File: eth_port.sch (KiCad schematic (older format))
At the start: 59 parts, among them J301 8P8C_LED_Shielded, U301 LAN8810

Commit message: Exported schematic PDF and BoM, the latter manually massaged. Added a couple missing part #s for big things which seemed important.
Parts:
- TR301: Part# (none) -> PT61020EL
- U301: Part# (none) -> LAN8810-AKZE
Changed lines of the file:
@@
 F 2 "myfp:QFN-72-1EP_10x10mm_P0.5mm_EP6x6mm_ThermalVias" H 4500 3250 50  0001 C CNN
 F 3 "" H 4500 3250 50  0001 C CNN
+F 4 "LAN8810-AKZE" H 4500 3250 50  0001 C CNN "Part#"
 	1    4500 3250
 	1    0    0    -1
@@
 F 2 "myfp:magnetics_PT61020E" H 8300 1450 50  0001 C CNN
 F 3 "" H 8300 2450 50  0001 C CNN
+F 4 "PT61020EL" H 8300 2450 50  0001 C CNN "Part#"
 	1    8300 2450
 	1    0    0    -1
@@
 	1    0    0    -1
 $EndComp
-Wire Bus Line
-	3200 3400 3200 4100
-Wire Bus Line
-	3200 2100 3200 2800
 $Comp
 L Device:C C210
@@
 	1    0    0    -1
 $EndComp
+Wire Bus Line
+	3200 3400 3200 4100
+Wire Bus Line
+	3200 2100 3200 2800
 $EndSCHEMATC

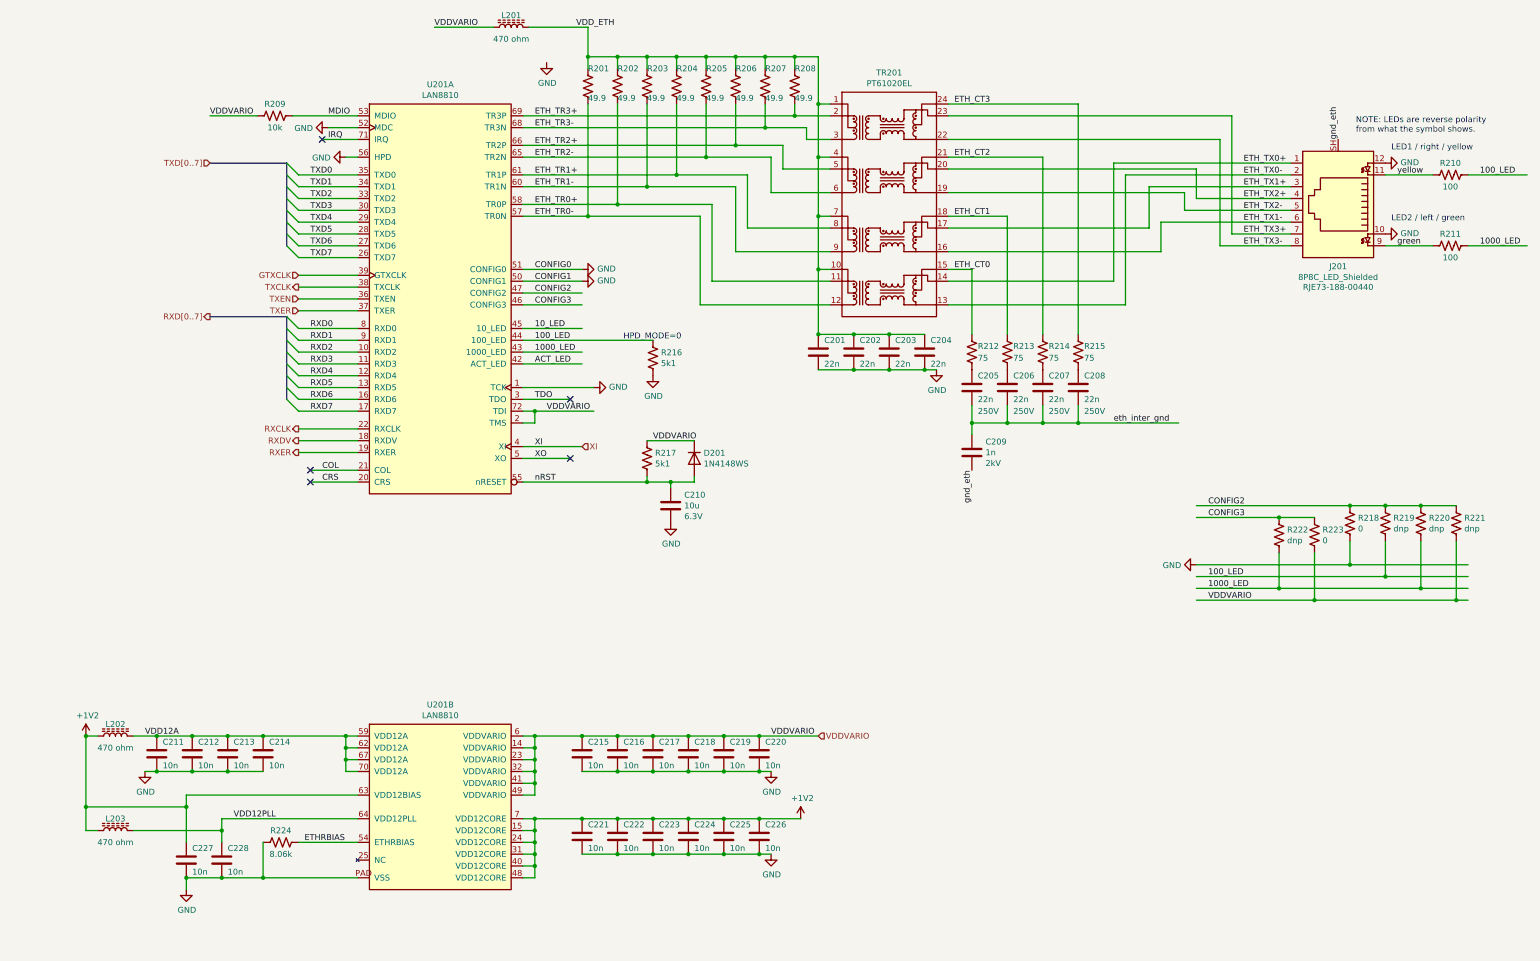
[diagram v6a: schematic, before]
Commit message: Started modifying the schematic to make a different flavor (JVC43B) based on the LAN8831 instead of LAN8810 chip.
This also involved:
- Adding series resistors to the PHY transmit wires (this probably should have
  been there in the A version too)
- Swapped out the 0603 decoupling caps for 0402 ones
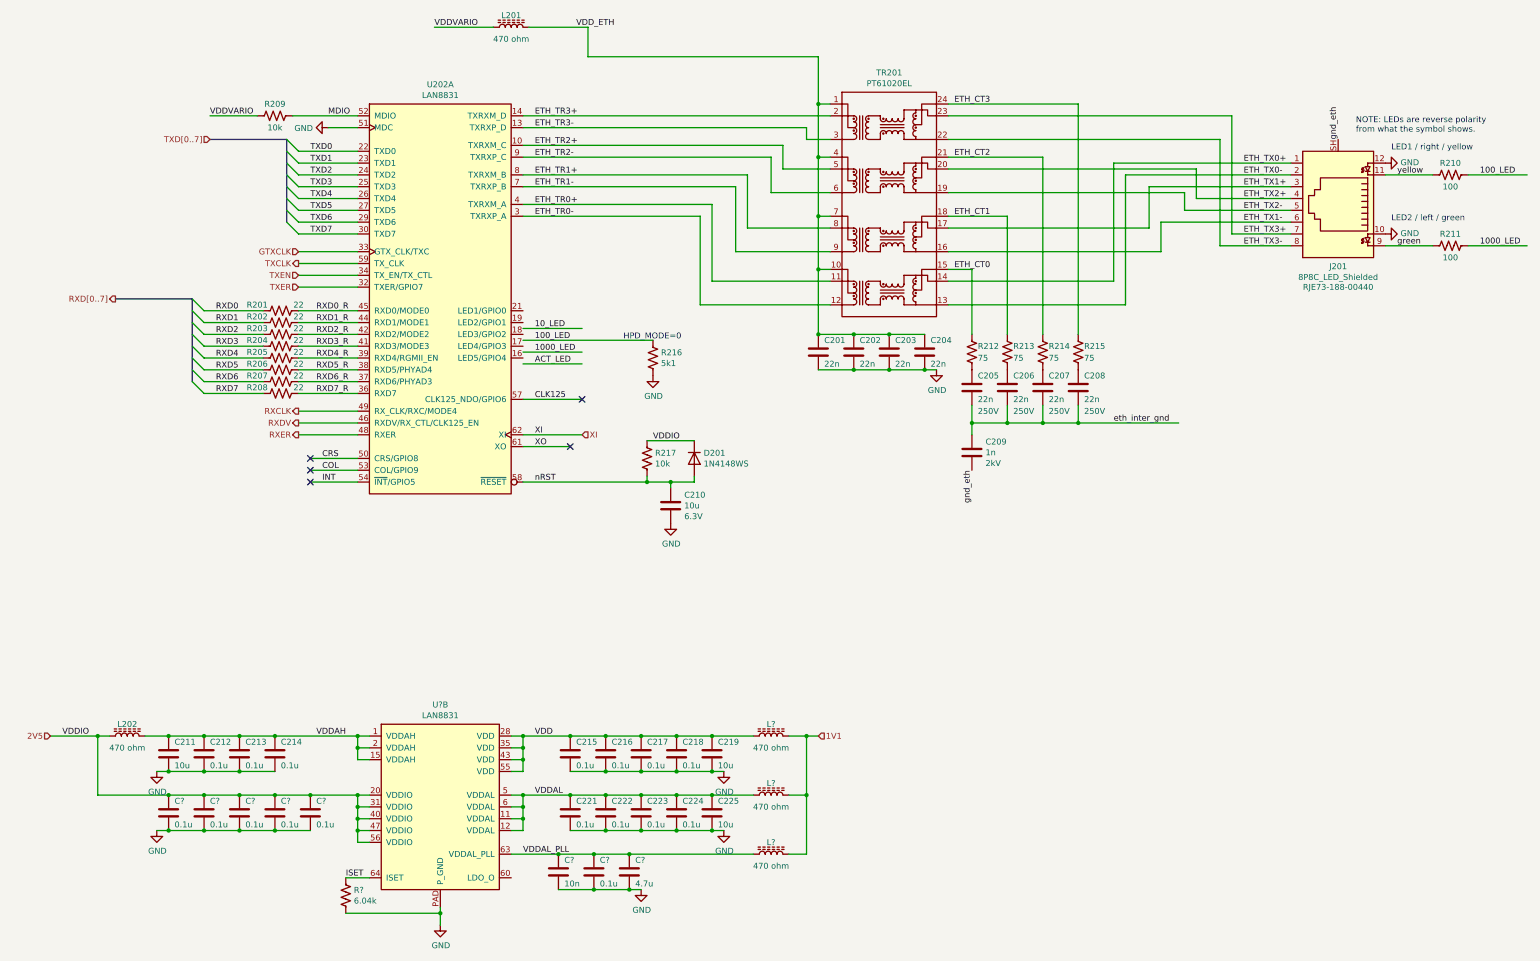
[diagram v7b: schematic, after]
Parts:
- removed C320, C326, C327, C328: 10n, Capacitor_SMD:C_0603_1608Metric, symbol Device:C
- removed L303: 470 ohm, Inductor_SMD:L_0603_1608Metric, symbol Device:L_Core_Ferrite
- removed R218, R223: 0, Resistor_SMD:R_0402_1005Metric, symbol Device:R_US
- removed R219, R220, R221, R222: dnp, Resistor_SMD:R_0402_1005Metric, symbol Device:R_US
- removed R301, R302, R303, R304, R305, R306, R307, R308: 49.9, Resistor_SMD:R_0603_1608Metric, symbol Device:R_US
- removed R324: 8.06k, Resistor_SMD:R_0603_1608Metric, symbol Device:R_US
- removed U301: LAN8810, myfp:QFN-72-1EP_10x10mm_P0.5mm_EP6x6mm_ThermalVias, symbol mysyms:LAN8810
- added C?: 10n, Capacitor_SMD:C_0603_1608Metric, symbol Device:C
- added C?: 0.1u, Capacitor_SMD:C_0603_1608Metric, symbol Device:C
- added C?: 4.7u, Capacitor_SMD:C_0603_1608Metric, symbol Device:C
- added C? (x5): 0.1u, Capacitor_SMD:C_0402_1005Metric, symbol Device:C
- added L? (x3): 470 ohm, Inductor_SMD:L_0603_1608Metric, symbol Device:L_Core_Ferrite
- added R201, R202, R203, R204, R205, R206, R207, R208: 22, Resistor_SMD:R_0402_1005Metric, symbol Device:R_US
- added R?: 6.04k, Resistor_SMD:R_0603_1608Metric, symbol Device:R_US
- added U202, U?: LAN8831, myfp:QFN-64-1EP_8x8mm_P0.4mm_EP6x6mm_ThermalVias, symbol mysyms:LAN8831
- C311, C319, C325: value 10n -> 10u
- C312, C313, C314, C315, C316, C317, C318, C321, C322, C323, C324: value 10n -> 0.1u
- R217: value 5k1 -> 10k
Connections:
- net labels added: 1V1, 2V5, CLK125, INT, ISET, RXD0_R, RXD1_R, RXD2_R, RXD3_R, RXD4_R, RXD5_R, RXD6_R, RXD7_R, VDD, VDDAH, VDDAL, VDDAL_PLL, VDDIO
- net labels removed: +1V2, CONFIG0, CONFIG1, CONFIG2, CONFIG3, ETHRBIAS, IRQ, TDO, VDD12A, VDD12PLL
- wire segments 275 -> 228
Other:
- moved on the sheet: C211, C212, C213, C214, C215, C216, C217, C218, C219, C221, C222, C223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

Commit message: Forward progress: - Ripped up a good chunk of the old place&route around the PHYs - Swizzled graphical placement of LAN8831 diff pair pins, to make the trace   routing be straight-thru.  This also involved swapping the polarity I'm   feeding into the magnetics.  Bonus: the magnetics-to-RJ45 is now straight,   instead of having to go around the back sides! - Adjusted some default trace spacings because of the tiny 0.4mm QFN:   - Switched default traces from 8mil to 7.8mil   - Switched diff pairs from 8.8/8.1 to 7.4/7.8 - Whoops, not all the 0.1uF decoupling caps were 0402 sized yet - Filled in a lot of specific vendor P/Ns for resistors & capacitors, to make   dealing with assembly houses easier
PHY1 has all its close-in decoupling caps placed & routed, PHY2 does not yet.
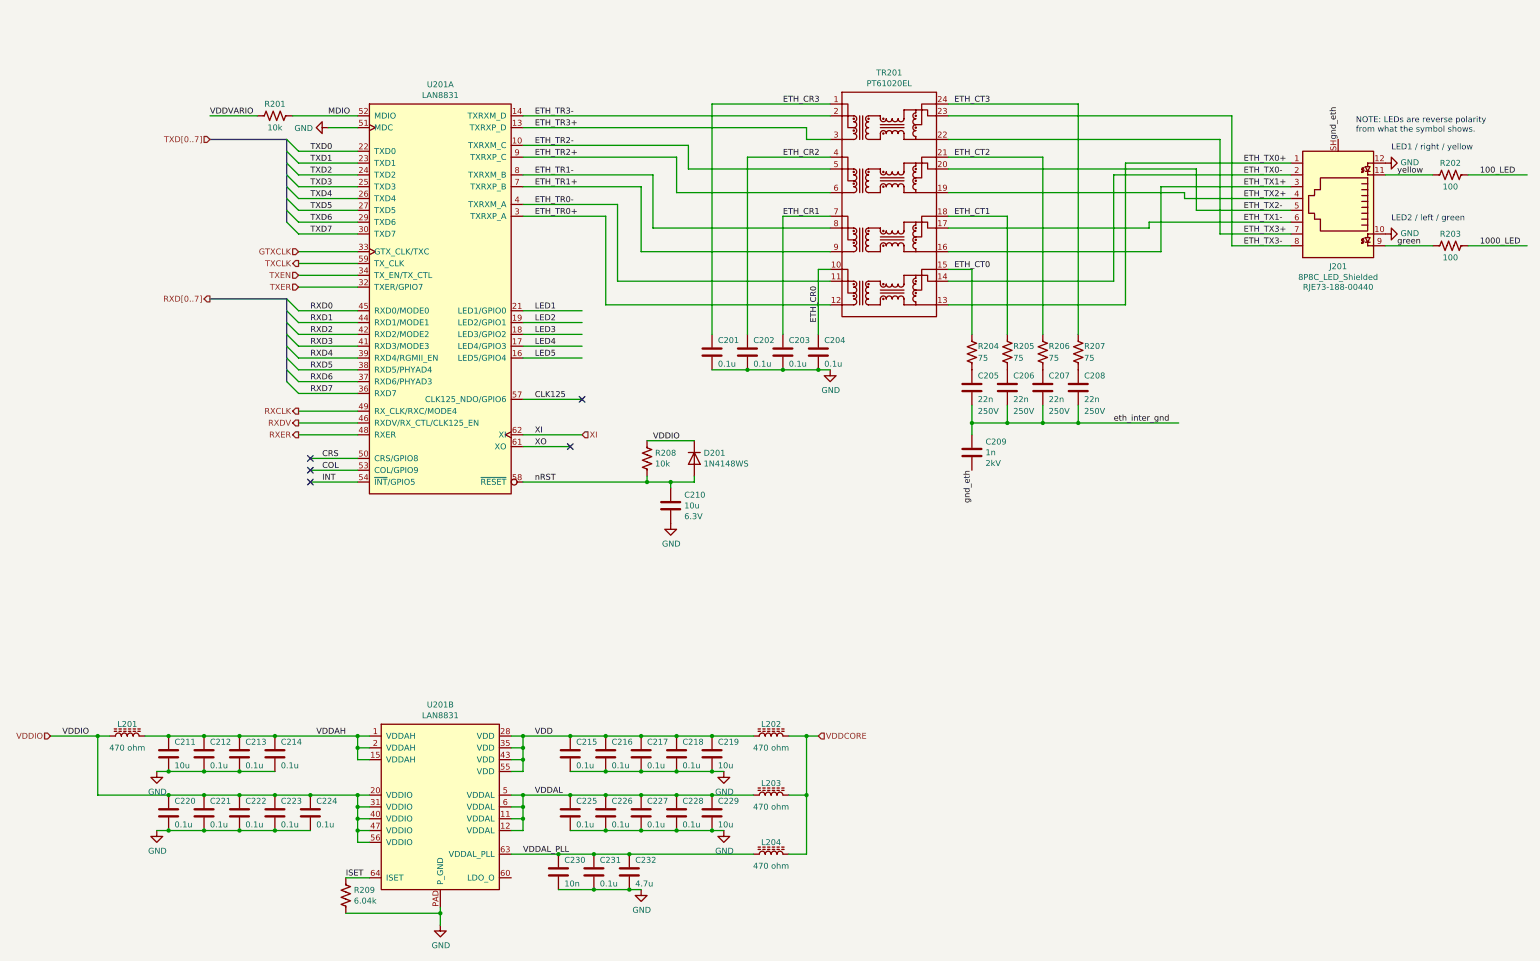
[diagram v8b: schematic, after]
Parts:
- removed L301: 470 ohm, Inductor_SMD:L_0603_1608Metric, symbol Device:L_Core_Ferrite
- removed R201, R202, R203, R204, R205, R206, R207, R208: 22, Resistor_SMD:R_0402_1005Metric, symbol Device:R_US
- removed R316: 5k1, Resistor_SMD:R_0603_1608Metric, symbol Device:R_US
- C205, C206, C207, C208: Part# CGA4J3X7R2E223K125AE -> CGA4J3X7R2E223K125AA
- C209: Part# (none) -> C1206X102KGRACAUTO
- C301, C302, C303, C304: value 22n -> 0.1u; footprint Capacitor_SMD:C_0603_1608Metric -> Capacitor_SMD:C_0402_1005Metric; Part# (none) -> CGA2B1X7R1C104K050BC
- C312, C313, C314, C315, C316, C317, C318: footprint Capacitor_SMD:C_0603_1608Metric -> Capacitor_SMD:C_0402_1005Metric; Part# (none) -> CGA2B1X7R1C104K050BC; Voltage 10V -> 16V
- C320, C321, C322, C323, C324: renamed from C?; Part# (none) -> CGA2B1X7R1C104K050BC; Voltage 10V -> 16V
- C325: renamed from C321; footprint Capacitor_SMD:C_0603_1608Metric -> Capacitor_SMD:C_0402_1005Metric; Part# (none) -> CGA2B1X7R1C104K050BC; Voltage 10V -> 16V
- C326: renamed from C322; footprint Capacitor_SMD:C_0603_1608Metric -> Capacitor_SMD:C_0402_1005Metric; Part# (none) -> CGA2B1X7R1C104K050BC; Voltage 10V -> 16V
- C327: renamed from C323; footprint Capacitor_SMD:C_0603_1608Metric -> Capacitor_SMD:C_0402_1005Metric; Part# (none) -> CGA2B1X7R1C104K050BC; Voltage 10V -> 16V
- C328: renamed from C324; footprint Capacitor_SMD:C_0603_1608Metric -> Capacitor_SMD:C_0402_1005Metric; Part# (none) -> CGA2B1X7R1C104K050BC; Voltage 10V -> 16V
- C330: renamed from C?; footprint Capacitor_SMD:C_0603_1608Metric -> Capacitor_SMD:C_0402_1005Metric
- C331: renamed from C?; footprint Capacitor_SMD:C_0603_1608Metric -> Capacitor_SMD:C_0402_1005Metric; Part# (none) -> CGA2B1X7R1C104K050BC; Voltage 10V -> 16V
- D201: Part# (none) -> 1N4148WS-E3-08
- R201: renamed from R209; Part# (none) -> ERJ-3EKF1002V
- R202: renamed from R210; Part# (none) -> ERJ-3EKF1000V
- R203: renamed from R211; Part# (none) -> ERJ-3EKF1000V
- R204: renamed from R212; Part# (none) -> ERJ-3EKF75R0V
- R205: renamed from R213; Part# (none) -> ERJ-3EKF75R0V
- R206: renamed from R214; Part# (none) -> ERJ-3EKF75R0V
- R207: renamed from R215; Part# (none) -> ERJ-3EKF75R0V
- R208: renamed from R217; Part# (none) -> ERJ-3EKF1002V
- R209: renamed from R?; Part# (none) -> ERJ-3EKF6041V
- gave numbers to parts that had none: 5
- renumbered C325 to C329, L302 to L301, U202 to U201
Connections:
- net labels added: ETH_CR0, ETH_CR1, ETH_CR2, ETH_CR3, LED1, LED2, LED3, LED4, LED5, VDDCORE
- net labels removed: 10_LED, 1V1, 2V5, ACT_LED, RXD0_R, RXD1_R, RXD2_R, RXD3_R, RXD4_R, RXD5_R, RXD6_R, RXD7_R, VDD_ETH
- wire segments 228 -> 213
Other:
- note removed: "HPD_MODE=0"
- moved on the sheet: C201, C202, C203, C204
